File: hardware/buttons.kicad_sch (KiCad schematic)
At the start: 27 parts, among them Q1 2N7002, Q2 2N7002, Q3 2N7002, Q4 2N7002, Q5 2N7002, Q6 2N7002

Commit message: Smaller high value caps. Standard R/C footprints instead of hand solder.
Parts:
- C14, C15, C16, C8, C9: footprint Capacitor_SMD:C_0603_1608Metric_Pad1.08x0.95mm_HandSolder -> Capacitor_SMD:C_0603_1608Metric; Comment X7R 16V -> X7R 10V; LCSC EMK107B7105KA-T -> (none)
- R10, R11, R12, R13, R14, R15, R16, R17, R18, R19, R20, R21, R6, R7, R8, R9: footprint Resistor_SMD:R_0603_1608Metric_Pad0.98x0.95mm_HandSolder -> Resistor_SMD:R_0603_1608Metric
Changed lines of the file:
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@@
       (effects (font (size 1.27 1.27)) (justify right))
     )
-    (property "Footprint" "Resistor_SMD:R_0603_1608Metric_Pad0.98x0.95mm_HandSolder" (id 2) (at 58.928 96.52 90)
+    (property "Footprint" "Resistor_SMD:R_0603_1608Metric" (id 2) (at 58.928 96.52 90)
       (effects (font (size 1.27 1.27)) hide)
     )
@@
     (property "Reference" "R13" (id 0) (at 46.99 97.79 90))
     (property "Value" "33k" (id 1) (at 46.99 100.33 90))
-    (property "Footprint" "Resistor_SMD:R_0603_1608Metric_Pad0.98x0.95mm_HandSolder" (id 2) (at 46.99 105.918 90)
+    (property "Footprint" "Resistor_SMD:R_0603_1608Metric" (id 2) (at 46.99 105.918 90)
       (effects (font (size 1.27 1.27)) hide)
     )
@@
     (property "Reference" "R16" (id 0) (at 133.35 133.35 90))
     (property "Value" "100" (id 1) (at 133.35 135.89 90))
-    (property "Footprint" "Resistor_SMD:R_0603_1608Metric_Pad0.98x0.95mm_HandSolder" (id 2) (at 133.35 141.478 90)
+    (property "Footprint" "Resistor_SMD:R_0603_1608Metric" (id 2) (at 133.35 141.478 90)
       (effects (font (size 1.27 1.27)) hide)
     )
@@
       (effects (font (size 1.27 1.27)) (justify left))
     )
-    (property "Footprint" "Capacitor_SMD:C_0603_1608Metric_Pad1.08x0.95mm_HandSolder" (id 2) (at 108.9152 68.58 0)
+    (property "Footprint" "Capacitor_SMD:C_0603_1608Metric" (id 2) (at 108.9152 68.58 0)
       (effects (font (size 1.27 1.27)) hide)
     )
@@
       (effects (font (size 1.27 1.27)) hide)
     )
-    (property "Comment" "X7R 16V" (id 4) (at 107.95 64.77 0)
-      (effects (font (size 1.27 1.27)) hide)
-    )
-    (property "LCSC" "EMK107B7105KA-T" (id 5) (at 107.95 64.77 0)
+    (property "Comment" "X7R 10V" (id 4) (at 107.95 64.77 0)
+      (effects (font (size 1.27 1.27)) hide)
+    )
+    (property "LCSC" "" (id 5) (at 107.95 64.77 0)
       (effects (font (size 1.27 1.27)) hide)
     )
@@
       (effects (font (size 1.27 1.27)) (justify right))
     )
-    (property "Footprint" "Resistor_SMD:R_0603_1608Metric_Pad0.98x0.95mm_HandSolder" (id 2) (at 130.048 96.52 90)
+    (property "Footprint" "Resistor_SMD:R_0603_1608Metric" (id 2) (at 130.048 96.52 90)
       (effects (font (size 1.27 1.27)) hide)
     )
@@
     (property "Reference" "R18" (id 0) (at 95.25 163.83 90))
     (property "Value" "100" (id 1) (at 95.25 166.37 90))
-    (property "Footprint" "Resistor_SMD:R_0603_1608Metric_Pad0.98x0.95mm_HandSolder" (id 2) (at 95.25 171.958 90)
+    (property "Footprint" "Resistor_SMD:R_0603_1608Metric" (id 2) (at 95.25 171.958 90)
       (effects (font (size 1.27 1.27)) hide)
     )
@@
       (effects (font (size 1.27 1.27)) (justify right))
     )
-    (property "Footprint" "Resistor_SMD:R_0603_1608Metric_Pad0.98x0.95mm_HandSolder" (id 2) (at 58.928 50.8 90)
+    (property "Footprint" "Resistor_SMD:R_0603_1608Metric" (id 2) (at 58.928 50.8 90)
       (effects (font (size 1.27 1.27)) hide)
     )
@@
     (property "Reference" "R7" (id 0) (at 46.99 52.07 90))
     (property "Value" "33k" (id 1) (at 46.99 54.61 90))
-    (property "Footprint" "Resistor_SMD:R_0603_1608Metric_Pad0.98x0.95mm_HandSolder" (id 2) (at 46.99 60.198 90)
+    (property "Footprint" "Resistor_SMD:R_0603_1608Metric" (id 2) (at 46.99 60.198 90)
       (effects (font (size 1.27 1.27)) hide)
     )
@@
     (property "Reference" "R15" (id 0) (at 95.25 133.35 90))
     (property "Value" "100" (id 1) (at 95.25 135.89 90))
-    (property "Footprint" "Resistor_SMD:R_0603_1608Metric_Pad0.98x0.95mm_HandSolder" (id 2) (at 95.25 141.478 90)
+    (property "Footprint" "Resistor_SMD:R_0603_1608Metric" (id 2) (at 95.25 141.478 90)
       (effects (font (size 1.27 1.27)) hide)
     )
@@
     (property "Reference" "R14" (id 0) (at 55.88 133.35 90))
     (property "Value" "100" (id 1) (at 55.88 135.89 90))
-    (property "Footprint" "Resistor_SMD:R_0603_1608Metric_Pad0.98x0.95mm_HandSolder" (id 2) (at 55.88 141.478 90)
+    (property "Footprint" "Resistor_SMD:R_0603_1608Metric" (id 2) (at 55.88 141.478 90)
       (effects (font (size 1.27 1.27)) hide)
     )
@@
       (effects (font (size 1.27 1.27)) (justify right))
     )
-    (property "Footprint" "Resistor_SMD:R_0603_1608Metric_Pad0.98x0.95mm_HandSolder" (id 2) (at 130.048 50.8 90)
+    (property "Footprint" "Resistor_SMD:R_0603_1608Metric" (id 2) (at 130.048 50.8 90)
       (effects (font (size 1.27 1.27)) hide)
     )
@@
       (effects (font (size 1.27 1.27)) (justify right))
     )
-    (property "Footprint" "Resistor_SMD:R_0603_1608Metric_Pad0.98x0.95mm_HandSolder" (id 2) (at 198.628 50.8 90)
+    (property "Footprint" "Resistor_SMD:R_0603_1608Metric" (id 2) (at 198.628 50.8 90)
       (effects (font (size 1.27 1.27)) hide)
     )
@@
       (effects (font (size 1.27 1.27)) (justify left))
     )
-    (property "Footprint" "Capacitor_SMD:C_0603_1608Metric_Pad1.08x0.95mm_HandSolder" (id 2) (at 37.7952 68.58 0)
+    (property "Footprint" "Capacitor_SMD:C_0603_1608Metric" (id 2) (at 37.7952 68.58 0)
       (effects (font (size 1.27 1.27)) hide)
     )
@@
       (effects (font (size 1.27 1.27)) hide)
     )
-    (property "Comment" "X7R 16V" (id 4) (at 36.83 64.77 0)
-      (effects (font (size 1.27 1.27)) hide)
-    )
-    (property "LCSC" "EMK107B7105KA-T" (id 5) (at 36.83 64.77 0)
+    (property "Comment" "X7R 10V" (id 4) (at 36.83 64.77 0)
+      (effects (font (size 1.27 1.27)) hide)
+    )
+    (property "LCSC" "" (id 5) (at 36.83 64.77 0)
       (effects (font (size 1.27 1.27)) hide)
     )
@@
       (effects (font (size 1.27 1.27)) (justify left))
     )
-    (property "Footprint" "Capacitor_SMD:C_0603_1608Metric_Pad1.08x0.95mm_HandSolder" (id 2) (at 37.7952 114.3 0)
+    (property "Footprint" "Capacitor_SMD:C_0603_1608Metric" (id 2) (at 37.7952 114.3 0)
       (effects (font (size 1.27 1.27)) hide)
     )
@@
       (effects (font (size 1.27 1.27)) hide)
     )
-    (property "Comment" "X7R 16V" (id 4) (at 36.83 110.49 0)
-      (effects (font (size 1.27 1.27)) hide)
-    )
-    (property "LCSC" "EMK107B7105KA-T" (id 5) (at 36.83 110.49 0)
+    (property "Comment" "X7R 10V" (id 4) (at 36.83 110.49 0)
+      (effects (font (size 1.27 1.27)) hide)
+    )
+    (property "LCSC" "" (id 5) (at 36.83 110.49 0)
       (effects (font (size 1.27 1.27)) hide)
     )
@@
     (property "Reference" "R17" (id 0) (at 55.88 163.83 90))
     (property "Value" "100" (id 1) (at 55.88 166.37 90))
-    (property "Footprint" "Resistor_SMD:R_0603_1608Metric_Pad0.98x0.95mm_HandSolder" (id 2) (at 55.88 171.958 90)
+    (property "Footprint" "Resistor_SMD:R_0603_1608Metric" (id 2) (at 55.88 171.958 90)
       (effects (font (size 1.27 1.27)) hide)
     )
@@
       (effects (font (size 1.27 1.27)) (justify left))
     )
-    (property "Footprint" "Capacitor_SMD:C_0603_1608Metric_Pad1.08x0.95mm_HandSolder" (id 2) (at 108.9152 114.3 0)
+    (property "Footprint" "Capacitor_SMD:C_0603_1608Metric" (id 2) (at 108.9152 114.3 0)
       (effects (font (size 1.27 1.27)) hide)
     )
@@
       (effects (font (size 1.27 1.27)) hide)
     )
-    (property "Comment" "X7R 16V" (id 4) (at 107.95 110.49 0)
-      (effects (font (size 1.27 1.27)) hide)
-    )
-    (property "LCSC" "EMK107B7105KA-T" (id 5) (at 107.95 110.49 0)
+    (property "Comment" "X7R 10V" (id 4) (at 107.95 110.49 0)
+      (effects (font (size 1.27 1.27)) hide)
+    )
+    (property "LCSC" "" (id 5) (at 107.95 110.49 0)
       (effects (font (size 1.27 1.27)) hide)
     )
@@
     (property "Reference" "R19" (id 0) (at 133.35 163.83 90))
     (property "Value" "100" (id 1) (at 133.35 166.37 90))
-    (property "Footprint" "Resistor_SMD:R_0603_1608Metric_Pad0.98x0.95mm_HandSolder" (id 2) (at 133.35 171.958 90)
+    (property "Footprint" "Resistor_SMD:R_0603_1608Metric" (id 2) (at 133.35 171.958 90)
       (effects (font (size 1.27 1.27)) hide)
     )
@@
     (property "Reference" "R21" (id 0) (at 118.11 97.79 90))
     (property "Value" "33k" (id 1) (at 118.11 100.33 90))
-    (property "Footprint" "Resistor_SMD:R_0603_1608Metric_Pad0.98x0.95mm_HandSolder" (id 2) (at 118.11 105.918 90)
+    (property "Footprint" "Resistor_SMD:R_0603_1608Metric" (id 2) (at 118.11 105.918 90)
       (effects (font (size 1.27 1.27)) hide)
     )
@@
       (effects (font (size 1.27 1.27)) (justify left))
     )
-    (property "Footprint" "Capacitor_SMD:C_0603_1608Metric_Pad1.08x0.95mm_HandSolder" (id 2) (at 177.4952 68.58 0)
+    (property "Footprint" "Capacitor_SMD:C_0603_1608Metric" (id 2) (at 177.4952 68.58 0)
       (effects (font (size 1.27 1.27)) hide)
     )
@@
       (effects (font (size 1.27 1.27)) hide)
     )
-    (property "Comment" "X7R 16V" (id 4) (at 176.53 64.77 0)
-      (effects (font (size 1.27 1.27)) hide)
-    )
-    (property "LCSC" "EMK107B7105KA-T" (id 5) (at 176.53 64.77 0)
+    (property "Comment" "X7R 10V" (id 4) (at 176.53 64.77 0)
+      (effects (font (size 1.27 1.27)) hide)
+    )
+    (property "LCSC" "" (id 5) (at 176.53 64.77 0)
       (effects (font (size 1.27 1.27)) hide)
     )
@@
     (property "Reference" "R9" (id 0) (at 118.11 52.07 90))
     (property "Value" "33k" (id 1) (at 118.11 54.61 90))
-    (property "Footprint" "Resistor_SMD:R_0603_1608Metric_Pad0.98x0.95mm_HandSolder" (id 2) (at 118.11 60.198 90)
+    (property "Footprint" "Resistor_SMD:R_0603_1608Metric" (id 2) (at 118.11 60.198 90)
       (effects (font (size 1.27 1.27)) hide)
     )
@@
     (property "Reference" "R11" (id 0) (at 186.69 52.07 90))
     (property "Value" "100" (id 1) (at 186.69 54.61 90))
-    (property "Footprint" "Resistor_SMD:R_0603_1608Metric_Pad0.98x0.95mm_HandSolder" (id 2) (at 186.69 60.198 90)
-      (effects (font (size 1.27 1.27)) hide)
-    )
+    (property "Footprint" "Resistor_SMD:R_0603_1608Metric" (id 2) (at 186.69 60.198 90)
+      (effects (font (size 1.27 1.27)) hide)
+    )

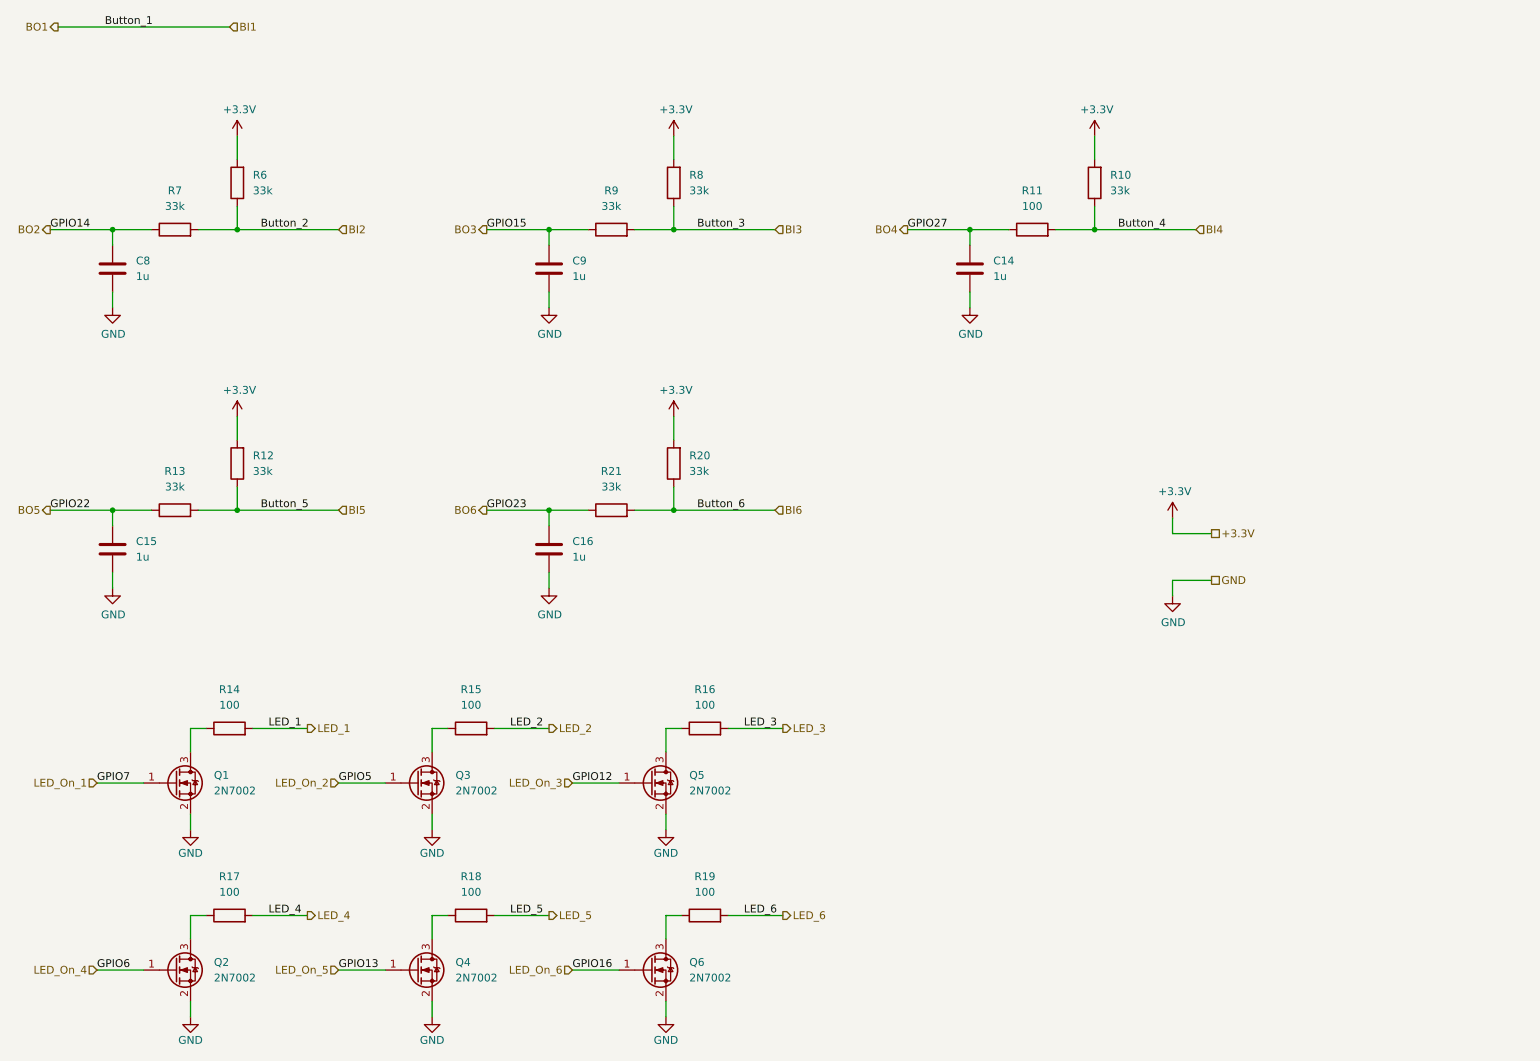
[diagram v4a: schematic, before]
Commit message: Fix all ERC warnings. Replace 4u7 capacitor in cut-off circuit by 100 nF cap and 10 kOhm in series to reduce stress on Raspi GPIO.
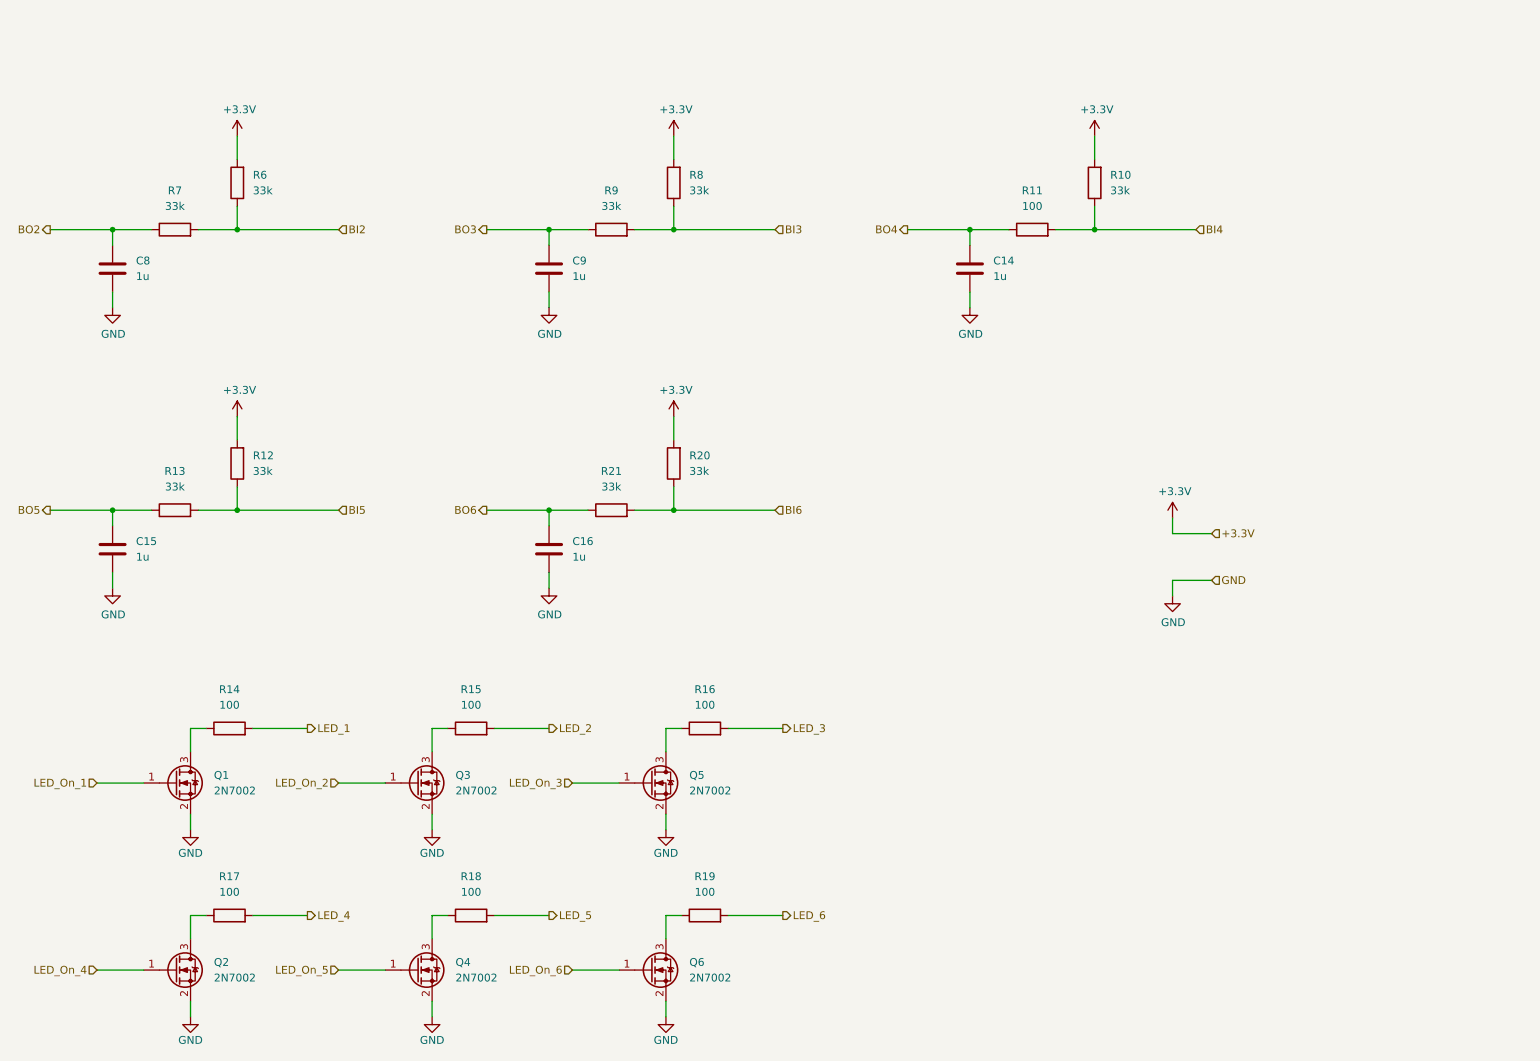
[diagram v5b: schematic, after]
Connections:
- net +3V3 renamed +3.3V
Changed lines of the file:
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@@
-    (stroke (width 0) (type default) (color 0 0 0 0))
-  )
-  (wire (pts (xy 27.94 25.4) (xy 55.88 25.4))
     (stroke (width 0) (type default) (color 0 0 0 0))
   )
@@
     (stroke (width 0) (type default) (color 0 0 0 0))
   )
-  (label "GPIO5" (at 73.66 148.59 0)
-    (effects (font (size 1.27 1.27)) (justify left bottom))
-  )
-  (label "GPIO7" (at 34.29 148.59 0)
-    (effects (font (size 1.27 1.27)) (justify left bottom))
-  )
-  (label "GPIO14" (at 26.67 58.42 0)
-    (effects (font (size 1.27 1.27)) (justify left bottom))
-  )
-  (label "GPIO23" (at 97.79 104.14 0)
-    (effects (font (size 1.27 1.27)) (justify left bottom))
-  )
-  (label "LED_3" (at 139.7 139.7 0)
-    (effects (font (size 1.27 1.27)) (justify left bottom))
-  )
-  (label "LED_1" (at 62.23 139.7 0)
-    (effects (font (size 1.27 1.27)) (justify left bottom))
-  )
-  (label "Button_6" (at 132.08 104.14 0)
-    (effects (font (size 1.27 1.27)) (justify left bottom))
-  )
-  (label "Button_5" (at 60.96 104.14 0)
-    (effects (font (size 1.27 1.27)) (justify left bottom))
-  )
-  (label "Button_3" (at 132.08 58.42 0)
-    (effects (font (size 1.27 1.27)) (justify left bottom))
-  )
-  (label "LED_4" (at 62.23 170.18 0)
-    (effects (font (size 1.27 1.27)) (justify left bottom))
-  )
-  (label "GPIO16" (at 111.76 179.07 0)
-    (effects (font (size 1.27 1.27)) (justify left bottom))
-  )
-  (label "GPIO13" (at 73.66 179.07 0)
-    (effects (font (size 1.27 1.27)) (justify left bottom))
-  )
-  (label "LED_5" (at 101.6 170.18 0)
-    (effects (font (size 1.27 1.27)) (justify left bottom))
-  )
-  (label "GPIO15" (at 97.79 58.42 0)
-    (effects (font (size 1.27 1.27)) (justify left bottom))
-  )
-  (label "GPIO12" (at 111.76 148.59 0)
-    (effects (font (size 1.27 1.27)) (justify left bottom))
-  )
-  (label "GPIO27" (at 166.37 58.42 0)
-    (effects (font (size 1.27 1.27)) (justify left bottom))
-  )
-  (label "Button_1" (at 35.56 25.4 0)
-    (effects (font (size 1.27 1.27)) (justify left bottom))
-  )
-  (label "Button_4" (at 200.66 58.42 0)
-    (effects (font (size 1.27 1.27)) (justify left bottom))
-  )
-  (label "LED_2" (at 101.6 139.7 0)
-    (effects (font (size 1.27 1.27)) (justify left bottom))
-  )
-  (label "GPIO22" (at 26.67 104.14 0)
-    (effects (font (size 1.27 1.27)) (justify left bottom))
-  )
-  (label "GPIO6" (at 34.29 179.07 0)
-    (effects (font (size 1.27 1.27)) (justify left bottom))
-  )
-  (label "Button_2" (at 60.96 58.42 0)
-    (effects (font (size 1.27 1.27)) (justify left bottom))
-  )
-  (label "LED_6" (at 139.7 170.18 0)
-    (effects (font (size 1.27 1.27)) (justify left bottom))
-  )
   (hierarchical_label "BI6" (shape input) (at 144.78 104.14 0)
     (effects (font (size 1.27 1.27)) (justify left))
@@
     (effects (font (size 1.27 1.27)) (justify right))
   )
-  (hierarchical_label "+3.3V" (shape passive) (at 215.9 107.95 0)
+  (hierarchical_label "+3.3V" (shape input) (at 215.9 107.95 0)
     (effects (font (size 1.27 1.27)) (justify left))
   )
@@
     (effects (font (size 1.27 1.27)) (justify right))
   )
-  (hierarchical_label "BI1" (shape input) (at 55.88 25.4 0)
-    (effects (font (size 1.27 1.27)) (justify left))
-  )
   (hierarchical_label "LED_On_4" (shape input) (at 34.29 179.07 180)
     (effects (font (size 1.27 1.27)) (justify right))
@@
     (effects (font (size 1.27 1.27)) (justify right))
   )
-  (hierarchical_label "GND" (shape passive) (at 215.9 115.57 0)
+  (hierarchical_label "GND" (shape input) (at 215.9 115.57 0)
     (effects (font (size 1.27 1.27)) (justify left))
   )
@@
     (effects (font (size 1.27 1.27)) (justify left))
   )
-  (hierarchical_label "BO1" (shape output) (at 27.94 25.4 180)
-    (effects (font (size 1.27 1.27)) (justify right))
-  )
   (hierarchical_label "BI5" (shape input) (at 73.66 104.14 0)

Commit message: Button resistors must be 100 Ohms
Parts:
- R13, R21, R7, R9: value 33k -> 100
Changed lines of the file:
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@@
     (in_bom yes) (on_board yes) (fields_autoplaced)
     (property "Reference" "R13" (id 0) (at 46.99 97.79 90))
-    (property "Value" "33k" (id 1) (at 46.99 100.33 90))
+    (property "Value" "100" (id 1) (at 46.99 100.33 90))
     (property "Footprint" "Resistor_SMD:R_0603_1608Metric" (id 2) (at 46.99 105.918 90)
       (effects (font (size 1.27 1.27)) hide)
@@
     (in_bom yes) (on_board yes) (fields_autoplaced)
     (property "Reference" "R7" (id 0) (at 46.99 52.07 90))
-    (property "Value" "33k" (id 1) (at 46.99 54.61 90))
+    (property "Value" "100" (id 1) (at 46.99 54.61 90))
     (property "Footprint" "Resistor_SMD:R_0603_1608Metric" (id 2) (at 46.99 60.198 90)
       (effects (font (size 1.27 1.27)) hide)
@@
     (in_bom yes) (on_board yes) (fields_autoplaced)
     (property "Reference" "R21" (id 0) (at 118.11 97.79 90))
-    (property "Value" "33k" (id 1) (at 118.11 100.33 90))
+    (property "Value" "100" (id 1) (at 118.11 100.33 90))
     (property "Footprint" "Resistor_SMD:R_0603_1608Metric" (id 2) (at 118.11 105.918 90)
       (effects (font (size 1.27 1.27)) hide)
@@
     (in_bom yes) (on_board yes) (fields_autoplaced)
     (property "Reference" "R9" (id 0) (at 118.11 52.07 90))
-    (property "Value" "33k" (id 1) (at 118.11 54.61 90))
+    (property "Value" "100" (id 1) (at 118.11 54.61 90))
     (property "Footprint" "Resistor_SMD:R_0603_1608Metric" (id 2) (at 118.11 60.198 90)
       (effects (font (size 1.27 1.27)) hide)
